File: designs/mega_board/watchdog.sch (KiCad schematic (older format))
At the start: 6 parts

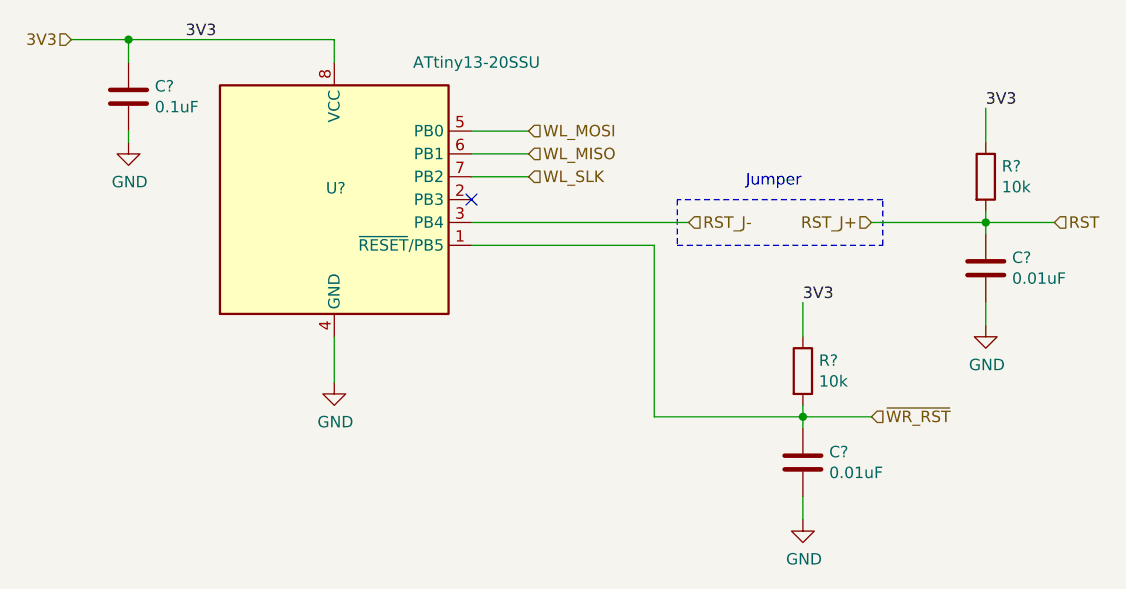
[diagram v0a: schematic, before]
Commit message: Enumerate components as is in eagle design.
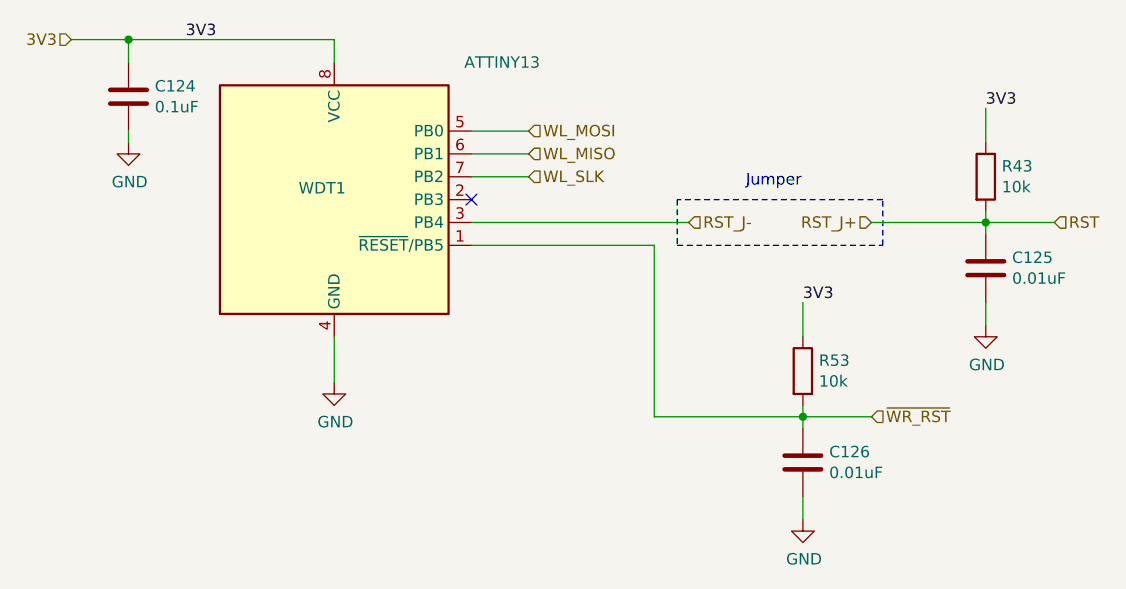
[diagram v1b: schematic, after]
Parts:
- C124, C125, C126: renamed from C?; footprint (none) -> LibreRouter_MegaBoard:C0402
- R43, R53: renamed from R?; footprint (none) -> LibreRouter_MegaBoard:R0402
- WDT1: renamed from U?; value ATtiny13-20SSU -> ATTINY13; footprint Package_SO:SOIC-8_3.9x4.9mm_P1.27mm -> LibreRouter_MegaBoard:S8S1
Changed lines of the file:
@@
 $Descr A4 11693 8268
 encoding utf-8
-Sheet 5 14
+Sheet 10 14
 Title "LibreRouter - Megaboard"
 Date "2019-06-26"
@@
 RST_J-
 $Comp
-L MCU_Microchip_ATtiny:ATtiny13-20SSU U?
+L MCU_Microchip_ATtiny:ATtiny13-20SSU WDT1
 U 1 1 5D14FFA1
 P 4700 3400
-F 0 "U?" H 4750 3450 50  0000 R CNN
-F 1 "ATtiny13-20SSU" H 5600 4000 50  0000 R CNN
-F 2 "Package_SO:SOIC-8_3.9x4.9mm_P1.27mm" H 4700 3400 50  0001 C CIN
+F 0 "WDT1" H 4750 3450 50  0000 R CNN
+F 1 "ATTINY13" H 5600 4000 50  0000 R CNN
+F 2 "LibreRouter_MegaBoard:S8S1" H 4700 3400 50  0001 C CIN
 F 3 "http://ww1.microchip.com/downloads/en/DeviceDoc/doc2535.pdf" H 4700 3400 50  0001 C CNN
 	1    4700 3400
@@
 $EndComp
 $Comp
-L Device:R R?
+L Device:R R53
 U 1 1 5D15016D
 P 6750 4150
-F 0 "R?" H 6820 4196 50  0000 L CNN
+F 0 "R53" H 6820 4196 50  0000 L CNN
 F 1 "10k" H 6820 4105 50  0000 L CNN
-F 2 "" V 6680 4150 50  0001 C CNN
+F 2 "LibreRouter_MegaBoard:R0402" V 6680 4150 50  0001 C CNN
 F 3 "~" H 6750 4150 50  0001 C CNN
 	1    6750 4150
@@
 $EndComp
 $Comp
-L Device:C C?
+L Device:C C126
 U 1 1 5D1501FA
 P 6750 4550
-F 0 "C?" H 6865 4596 50  0000 L CNN
+F 0 "C126" H 6865 4596 50  0000 L CNN
 F 1 "0.01uF" H 6865 4505 50  0000 L CNN
-F 2 "" H 6788 4400 50  0001 C CNN
+F 2 "LibreRouter_MegaBoard:C0402" H 6788 4400 50  0001 C CNN
 F 3 "~" H 6750 4550 50  0001 C CNN
 	1    6750 4550
@@
 $EndComp
 $Comp
-L power:GND #PWR?
+L power:GND #PWR0169
 U 1 1 5D150451
 P 4700 4200
-F 0 "#PWR?" H 4700 3950 50  0001 C CNN
+F 0 "#PWR0169" H 4700 3950 50  0001 C CNN
 F 1 "GND" H 4705 4027 50  0000 C CNN
 F 2 "" H 4700 4200 50  0001 C CNN
@@
 $EndComp
 $Comp
-L power:GND #PWR?
+L power:GND #PWR0170
 U 1 1 5D15046D
 P 6750 4800
-F 0 "#PWR?" H 6750 4550 50  0001 C CNN
+F 0 "#PWR0170" H 6750 4550 50  0001 C CNN
 F 1 "GND" H 6755 4627 50  0000 C CNN
 F 2 "" H 6750 4800 50  0001 C CNN
@@
 	6750 4350 6750 4300
 $Comp
-L Device:R R?
+L Device:R R43
 U 1 1 5D150638
 P 7550 3300
-F 0 "R?" H 7620 3346 50  0000 L CNN
+F 0 "R43" H 7620 3346 50  0000 L CNN
 F 1 "10k" H 7620 3255 50  0000 L CNN
-F 2 "" V 7480 3300 50  0001 C CNN
+F 2 "LibreRouter_MegaBoard:R0402" V 7480 3300 50  0001 C CNN
 F 3 "~" H 7550 3300 50  0001 C CNN
 	1    7550 3300
@@
 $EndComp
 $Comp
-L Device:C C?
+L Device:C C125
 U 1 1 5D15063F
 P 7550 3700
-F 0 "C?" H 7665 3746 50  0000 L CNN
+F 0 "C125" H 7665 3746 50  0000 L CNN
 F 1 "0.01uF" H 7665 3655 50  0000 L CNN
-F 2 "" H 7588 3550 50  0001 C CNN
+F 2 "LibreRouter_MegaBoard:C0402" H 7588 3550 50  0001 C CNN
 F 3 "~" H 7550 3700 50  0001 C CNN
 	1    7550 3700
@@
 $EndComp
 $Comp
-L power:GND #PWR?
+L power:GND #PWR0171
 U 1 1 5D150646
 P 7550 3950
-F 0 "#PWR?" H 7550 3700 50  0001 C CNN
+F 0 "#PWR0171" H 7550 3700 50  0001 C CNN
 F 1 "GND" H 7555 3777 50  0000 C CNN
 F 2 "" H 7550 3950 50  0001 C CNN
@@
 	7550 3500 7550 3450
 $Comp
-L Device:C C?
+L Device:C C124
 U 1 1 5D1B5630
 P 3800 2950
-F 0 "C?" H 3915 2996 50  0000 L CNN
+F 0 "C124" H 3915 2996 50  0000 L CNN
 F 1 "0.1uF" H 3915 2905 50  0000 L CNN
-F 2 "" H 3838 2800 50  0001 C CNN
+F 2 "LibreRouter_MegaBoard:C0402" H 3838 2800 50  0001 C CNN
 F 3 "~" H 3800 2950 50  0001 C CNN
 	1    3800 2950
@@
 $EndComp
 $Comp
-L power:GND #PWR?
+L power:GND #PWR0172
 U 1 1 5D1B56C8
 P 3800 3150
-F 0 "#PWR?" H 3800 2900 50  0001 C CNN
+F 0 "#PWR0172" H 3800 2900 50  0001 C CNN
 F 1 "GND" H 3805 2977 50  0000 C CNN
 F 2 "" H 3800 3150 50  0001 C CNN

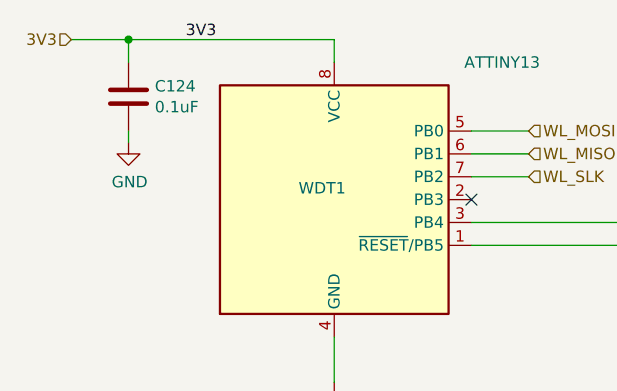
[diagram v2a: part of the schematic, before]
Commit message: Add capacitor definito to BOM
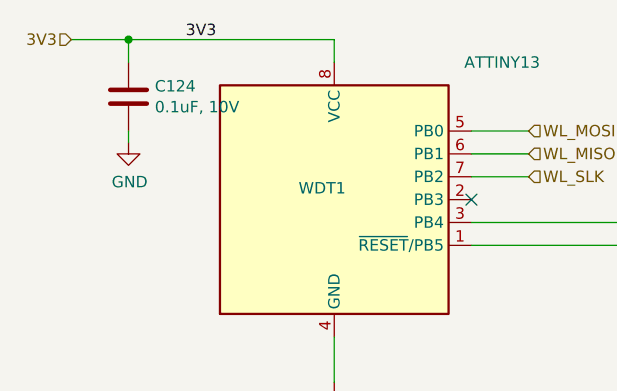
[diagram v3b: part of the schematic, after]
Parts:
- C124: value 0.1uF -> 0.1uF, 10V; Manufacturer (none) -> Murata Electronics; Manufacturer PN (none) -> GCM155R71A104KA55D; Supplier (none) -> DigiKey; Supplier PN (none) -> 490-16434-6-ND
- C125, C126: Manufacturer (none) -> Murata Electronics; Manufacturer PN (none) -> GRM155R71H103KA88J; Supplier (none) -> DigiKey; Supplier PN (none) -> 490-6351-6-ND
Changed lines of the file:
@@
 F 2 "LibreRouter_MegaBoard:C0402" H 6788 4400 50  0001 C CNN
 F 3 "~" H 6750 4550 50  0001 C CNN
+F 4 "DigiKey" H 6750 4550 50  0001 C CNN "Supplier"
+F 5 "Murata Electronics" H 6750 4550 50  0001 C CNN "Manufacturer"
+F 6 "GRM155R71H103KA88J" H 6750 4550 50  0001 C CNN "Manufacturer PN"
+F 7 "490-6351-6-ND" H 6750 4550 50  0001 C CNN "Supplier PN"
 	1    6750 4550
 	1    0    0    -1
@@
 F 2 "LibreRouter_MegaBoard:C0402" H 7588 3550 50  0001 C CNN
 F 3 "~" H 7550 3700 50  0001 C CNN
+F 4 "DigiKey" H 7550 3700 50  0001 C CNN "Supplier"
+F 5 "Murata Electronics" H 7550 3700 50  0001 C CNN "Manufacturer"
+F 6 "GRM155R71H103KA88J" H 7550 3700 50  0001 C CNN "Manufacturer PN"
+F 7 "490-6351-6-ND" H 7550 3700 50  0001 C CNN "Supplier PN"
 	1    7550 3700
 	1    0    0    -1
@@
 P 3800 2950
 F 0 "C124" H 3915 2996 50  0000 L CNN
-F 1 "0.1uF" H 3915 2905 50  0000 L CNN
+F 1 "0.1uF, 10V" H 3915 2905 50  0000 L CNN
 F 2 "LibreRouter_MegaBoard:C0402" H 3838 2800 50  0001 C CNN
 F 3 "~" H 3800 2950 50  0001 C CNN
+F 4 "Murata Electronics" H 3800 2950 50  0001 C CNN "Manufacturer"
+F 5 "GCM155R71A104KA55D" H 3800 2950 50  0001 C CNN "Manufacturer PN"
+F 6 "DigiKey" H 3800 2950 50  0001 C CNN "Supplier"
+F 7 "490-16434-6-ND" H 3800 2950 50  0001 C CNN "Supplier PN"
 	1    3800 2950
 	1    0    0    -1

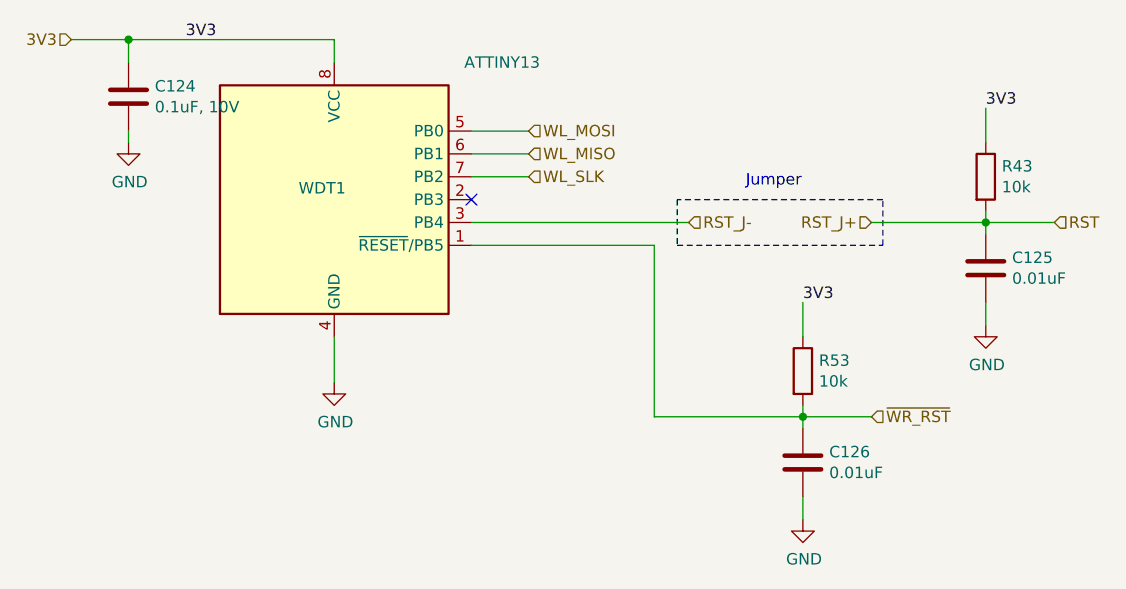
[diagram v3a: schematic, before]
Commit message: Add BOM definition to all resistors
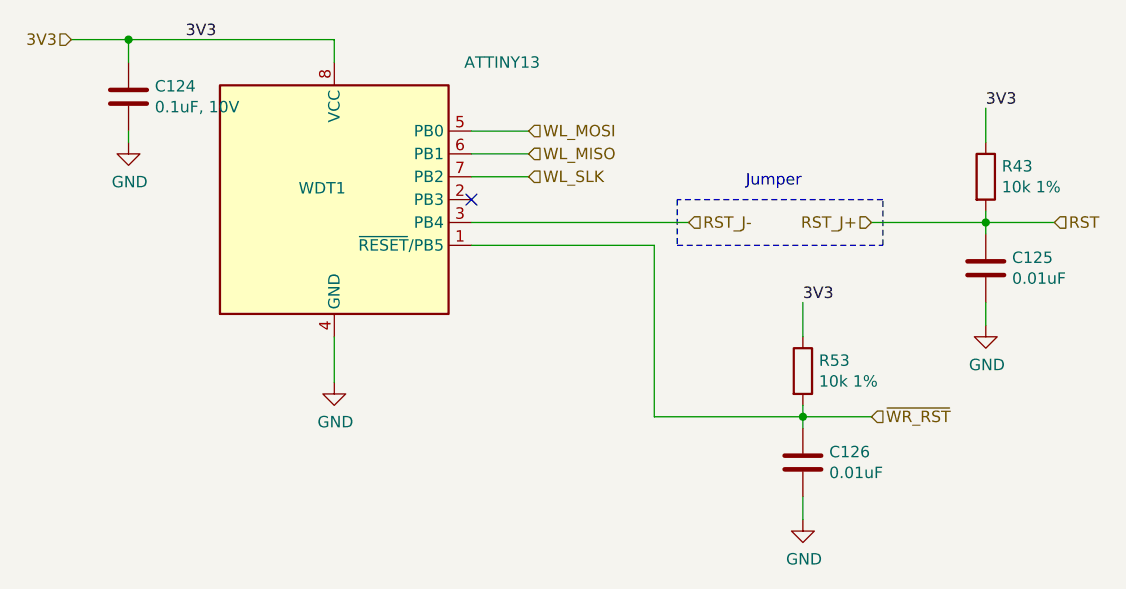
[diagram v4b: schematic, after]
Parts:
- R43, R53: value 10k -> 10k 1%; Manufacturer (none) -> Panasonic Electronic Components; Manufacturer PN (none) -> ERJ-PA2F1002X; Supplier (none) -> DigiKey; Supplier PN (none) -> P17230DKR-ND
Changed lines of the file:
@@
 P 6750 4150
 F 0 "R53" H 6820 4196 50  0000 L CNN
-F 1 "10k" H 6820 4105 50  0000 L CNN
+F 1 "10k 1%" H 6820 4105 50  0000 L CNN
 F 2 "LibreRouter_MegaBoard:R0402" V 6680 4150 50  0001 C CNN
 F 3 "~" H 6750 4150 50  0001 C CNN
+F 4 "Panasonic Electronic Components" H 6750 4150 50  0001 C CNN "Manufacturer"
+F 5 "ERJ-PA2F1002X" H 6750 4150 50  0001 C CNN "Manufacturer PN"
+F 6 "DigiKey" H 6750 4150 50  0001 C CNN "Supplier"
+F 7 "P17230DKR-ND" H 6750 4150 50  0001 C CNN "Supplier PN"
 	1    6750 4150
 	1    0    0    -1
@@
 P 7550 3300
 F 0 "R43" H 7620 3346 50  0000 L CNN
-F 1 "10k" H 7620 3255 50  0000 L CNN
+F 1 "10k 1%" H 7620 3255 50  0000 L CNN
 F 2 "LibreRouter_MegaBoard:R0402" V 7480 3300 50  0001 C CNN
 F 3 "~" H 7550 3300 50  0001 C CNN
+F 4 "Panasonic Electronic Components" H 7550 3300 50  0001 C CNN "Manufacturer"
+F 5 "ERJ-PA2F1002X" H 7550 3300 50  0001 C CNN "Manufacturer PN"
+F 6 "DigiKey" H 7550 3300 50  0001 C CNN "Supplier"
+F 7 "P17230DKR-ND" H 7550 3300 50  0001 C CNN "Supplier PN"
 	1    7550 3300
 	1    0    0    -1

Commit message: Add BOM definition for components. We need more iformation for all the components that are not defined.
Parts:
- WDT1: Manufacturer (none) -> Microchip Technology; Manufacturer PN (none) -> ATTINY13A-SSUR; Supplier (none) -> DigiKey; Supplier PN (none) -> ATTINY13A-SSURDKR-ND
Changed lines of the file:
@@
 F 2 "LibreRouter_MegaBoard:S8S1" H 4700 3400 50  0001 C CIN
 F 3 "http://ww1.microchip.com/downloads/en/DeviceDoc/doc2535.pdf" H 4700 3400 50  0001 C CNN
+F 4 "Microchip Technology" H 4700 3400 50  0001 C CNN "Manufacturer"
+F 5 "ATTINY13A-SSUR" H 4700 3400 50  0001 C CNN "Manufacturer PN"
+F 6 "DigiKey" H 4700 3400 50  0001 C CNN "Supplier"
+F 7 "ATTINY13A-SSURDKR-ND" H 4700 3400 50  0001 C CNN "Supplier PN"
 	1    4700 3400
 	1    0    0    -1

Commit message: Kicad madness
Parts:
- WDT1: symbol MCU_Microchip_ATtiny:ATtiny13-20SSU -> LibreRouter_MegaBoard-rescue:ATtiny13-20SSU-MCU_Microchip_ATtiny
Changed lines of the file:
@@
 EESchema Schematic File Version 4
-LIBS:LibreRouter_MegaBoard-cache
 EELAYER 30 0
 EELAYER END
@@
 RST_J-
 $Comp
-L MCU_Microchip_ATtiny:ATtiny13-20SSU WDT1
+L LibreRouter_MegaBoard-rescue:ATtiny13-20SSU-MCU_Microchip_ATtiny WDT1
 U 1 1 5D14FFA1
 P 4700 3400
